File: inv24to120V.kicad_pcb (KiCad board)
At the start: 2 copper layers, 105 x 155 mm, 133 parts, among them IC1 FSAM50SM60A, J1 Conn_02x13_Odd_Even_MountingP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, J10 Screw_Terminal_01x01, J11 Screw_Terminal_01x01, J12 Screw_Terminal_01x01, J2 Conn_02x13_Odd_Even_MountingP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, J3 Screw_Terminal_01x01, J4 Conn_02x05_Odd_Even_MountingP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, J5 Screw_Terminal_01x02, J6 Screw_Terminal_01x03, J7 Screw_Terminal_01x03, J8 Screw_Terminal_01x03, J9 Screw_Terminal_01x02, K1 J0971CS5VDC.45, Q1 IRFZ44NPBF, Q2 IRFZ44NPBF, Q3 2SC1815, Q4 2SC1815, Q5 2SA1015, Q6 2SA1015, Q7 2SC1815, U1 ESP32-DEVKITC-32D, U10 PC817, U2 LM2576HVT-5, U3 ACS712ELCTR30AT, U4 ACS712ELCTR30AT, U5 LM2576HVT-5, U6 ISO7340CDW, U7 ISO7340CDW, U8 AMC1300BDWVR, U9 PC817

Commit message: start rout
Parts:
- removed J1, J2: Conn_02x13_Odd_Even_MountingPin, Connector_IDC:IDC-Header_2x13_P2.54mm_Vertical
- removed J10, J11, J12, J3: Screw_Terminal_01x01, TerminalBlock_Wuerth:Wuerth_REDCUBE-THR_WP-THRBU_74650073_THR
- C10, C11, C12, C24, C25, C26, C27, C28, C29, C30, C31, C33, C34, C5, C6, C7, C8, C9: footprint Capacitor_SMD:C_0805_2012Metric -> Capacitor_SMD:C_0805_2012Metric_Pad1.18x1.45mm_HandSolder
- C13, C14, C15: footprint Capacitor_SMD:C_0805_2012Metric -> Capacitor_SMD:C_1206_3216Metric_Pad1.33x1.80mm_HandSolder
- R10, R22, R23, R24, R25, R26, R27, R28, R29, R30, R31, R32, R33, R34, R35, R36, R37, R7, R8, R9: footprint Resistor_SMD:R_0805_2012Metric -> Resistor_SMD:R_0805_2012Metric_Pad1.20x1.40mm_HandSolder
- R40, R44: footprint Resistor_THT:R_Axial_DIN0207_L6.3mm_D2.5mm_P10.16mm_Horizontal -> Resistor_SMD:R_0805_2012Metric_Pad1.20x1.40mm_HandSolder
- U1: footprint inv24VLib:MODULE_ESP32-DEVKITC-32D -> Connector_PinSocket_2.54mm:PinSocket_2x20_P2.54mm_Vertical
- moved J6 208.6 mm to (149.0, 160.0)
- moved Q7 204.7 mm to (127.5, 166.0)
- moved BX1 204.1 mm to (140.8, 175.0)
- moved D7 195.0 mm to (112.9, 176.0)
- moved BX2 190.3 mm to (126.9, 175.0)
- moved R42 181.8 mm to (135.0, 160.8), turned to -90 degrees
- moved R48 180.6 mm to (139.0, 161.0), turned to -90 degrees
- moved U9 162.5 mm to (114.2, 168.7)
- moved R46 162.0 mm to (109.8, 164.0)
- moved R45 158.4 mm to (95.8, 164.0)
- moved J9 158.1 mm to (102.0, 175.1), turned to 90 degrees
- moved K1 151.1 mm to (80.7, 143.7)
- moved R47 146.3 mm to (93.0, 177.0), turned to 90 degrees
- moved U10 139.7 mm to (116.3, 85.2), turned to -90 degrees
- moved C13 127.8 mm to (84.0, 71.5), turned to 180 degrees
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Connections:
- BX4 pad 2: VTH_IPM1 -> VTH_IPM
- BX6 pad 1: TEMPERATURE_IPM2 -> TEMPERATURE_IPM
- C33 pad 2: VTH_IPM1 -> VTH_IPM
- C34 pad 2: TEMPERATURE_IPM2 -> TEMPERATURE_IPM
- C35 pad 1: VTH_IPM1 -> VTH_IPM
- D8 pad 2: 150V_OUT1 -> 150V_OUT
- IC1 pad 16: unconnected-(IC1-COM(H)-Pad16) -> GNDPWR
- IC1 pad 24: VTH_IPM2 -> VTH_IPM
- IC1 pad 32: 150V_OUT -> VBUS
- L4 pad 1: Net-(J12-Pin_1) -> VBUS
- R10 pad 2: I_Vphase2 -> I_Vphase
- R17 pad 2: Net-(J12-Pin_1) -> VBUS
- R19 pad 1: GNDPWR1 -> GNDPWR
- R29 pad 1: UH2 -> Net-(U6-OUTA)
- R30 pad 1: VH2 -> Net-(U6-OUTB)
- R31 pad 1: WH2 -> Net-(U6-OUTC)
- R32 pad 1: UL2 -> Net-(U7-OUTA)
- R33 pad 1: VL2 -> Net-(U7-OUTB)
- R34 pad 1: WL2 -> Net-(U7-OUTC)
- R40 pad 2: TEMPERATURE_IPM2 -> TEMPERATURE_IPM
- R44 pad 2: FAULT_IPM2 -> FAULT_IPM
- R7 pad 1: I_Uphase2 -> I_Uphase
- R8 pad 1: I_Vphase2 -> I_Vphase
- R9 pad 2: I_Uphase2 -> I_Uphase
- U10 pad 4: FAULT_IPM2 -> FAULT_IPM
- U6 pad 12: WH1 -> Net-(U6-OUTC)
- U6 pad 13: VH1 -> Net-(U6-OUTB)
- U6 pad 14: UH1 -> Net-(U6-OUTA)
- U7 pad 12: WL1 -> Net-(U7-OUTC)
- U7 pad 13: VL1 -> Net-(U7-OUTB)
- U7 pad 14: UL1 -> Net-(U7-OUTA)
- U8 pad 3: GNDPWR1 -> GNDPWR
- X1 pad 12: GNDPWR1 -> GNDPWR
- X1 pad 13: GNDPWR1 -> GNDPWR
- X1 pad 15: 150V_OUT1 -> 150V_OUT
- X1 pad 16: 150V_OUT1 -> 150V_OUT

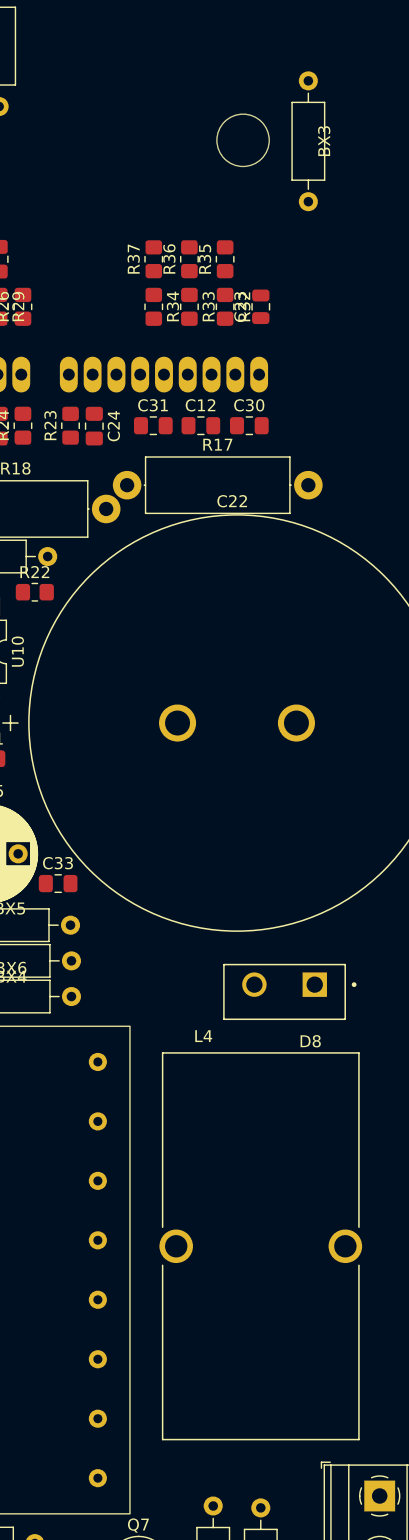
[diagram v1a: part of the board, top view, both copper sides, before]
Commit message: add class name
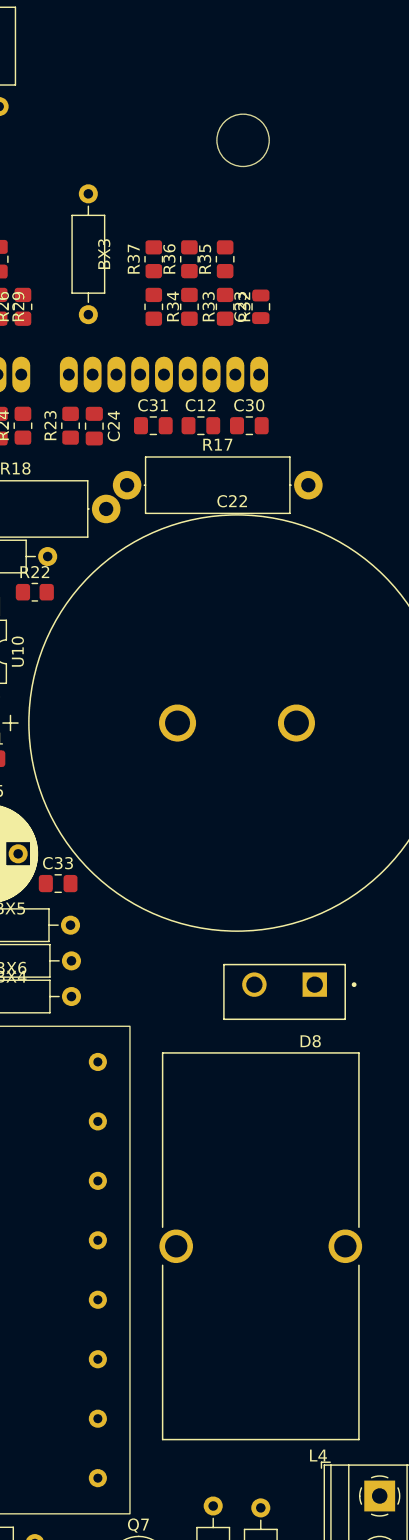
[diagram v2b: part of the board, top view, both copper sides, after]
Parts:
- moved BX3 20.8 mm to (124.5, 60.7)
- turned L4 to 180 degrees
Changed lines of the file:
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@@
   )
   (footprint "inv24VLib:IND_HCTI-10-20.0" (layer "F.Cu")
-    (at 139 139)
+    (at 139 139 180)
     (property "Sheetfile" "inv24to120V.kicad_sch")
     (property "Sheetname" "")
@@
     (fp_line (start 8.255 16.256) (end -8.255 16.256)
       (stroke (width 0.127) (type solid)) (layer "F.Fab"))
-    (pad "1" thru_hole circle (at -7.112 0) (size 2.82 2.82) (drill 1.88) (layers "*.Cu" "*.Mask")
+    (pad "1" thru_hole circle (at -7.112 0 180) (size 2.82 2.82) (drill 1.88) (layers "*.Cu" "*.Mask")
       (net 80 "VBUS") (pinfunction "1") (pintype "passive") (solder_mask_margin 0.102))
-    (pad "2" thru_hole circle (at 7.112 0) (size 2.82 2.82) (drill 1.88) (layers "*.Cu" "*.Mask")
+    (pad "2" thru_hole circle (at 7.112 0 180) (size 2.82 2.82) (drill 1.88) (layers "*.Cu" "*.Mask")
       (net 87 "Net-(D8-K)") (pinfunction "2") (pintype "passive") (solder_mask_margin 0.102))
     (model "${KIPRJMOD}/inv24VLib/ATCA-08-471M-V.STEP"
@@
   )
   (footprint "Resistor_THT:R_Axial_DIN0207_L6.3mm_D2.5mm_P10.16mm_Horizontal" (layer "F.Cu")
-    (at 143 51.16 90)
+    (at 124.5 60.66 90)
     (descr "Resistor, Axial_DIN0207 series, Axial, Horizontal, pin pitch=10.16mm, 0.25W = 1/4W, length*diameter=6.3*2.5mm^2, http://cdn-reichelt.de/documents/datenblatt/B400/1_4W%23YAG.pdf")
     (tags "Resistor Axial_DIN0207 series Axial Horizontal pin pitch 10.16mm 0.25W = 1/4W length 6.3mm diameter 2.5mm")

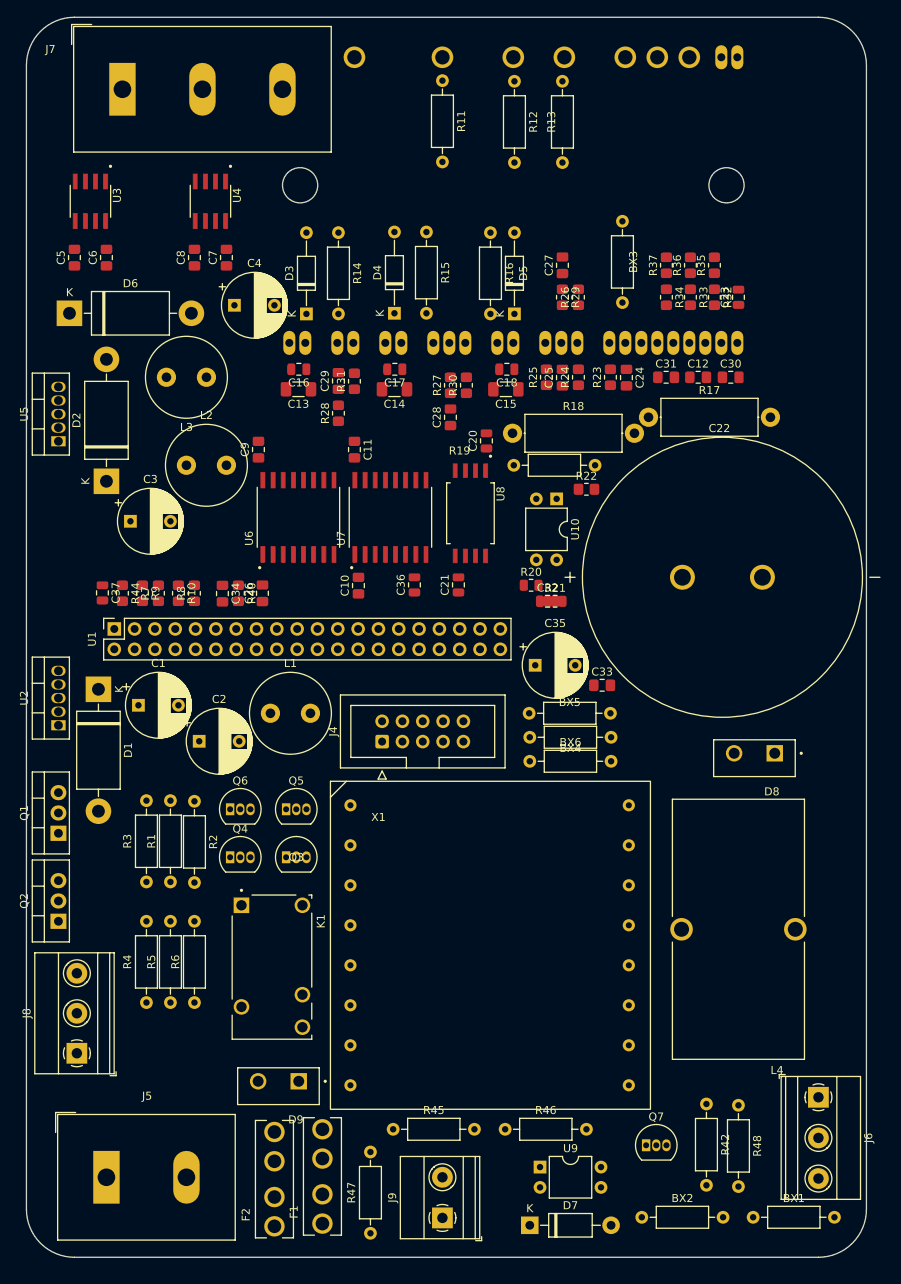
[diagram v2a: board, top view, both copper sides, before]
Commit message: remove aux addon connect
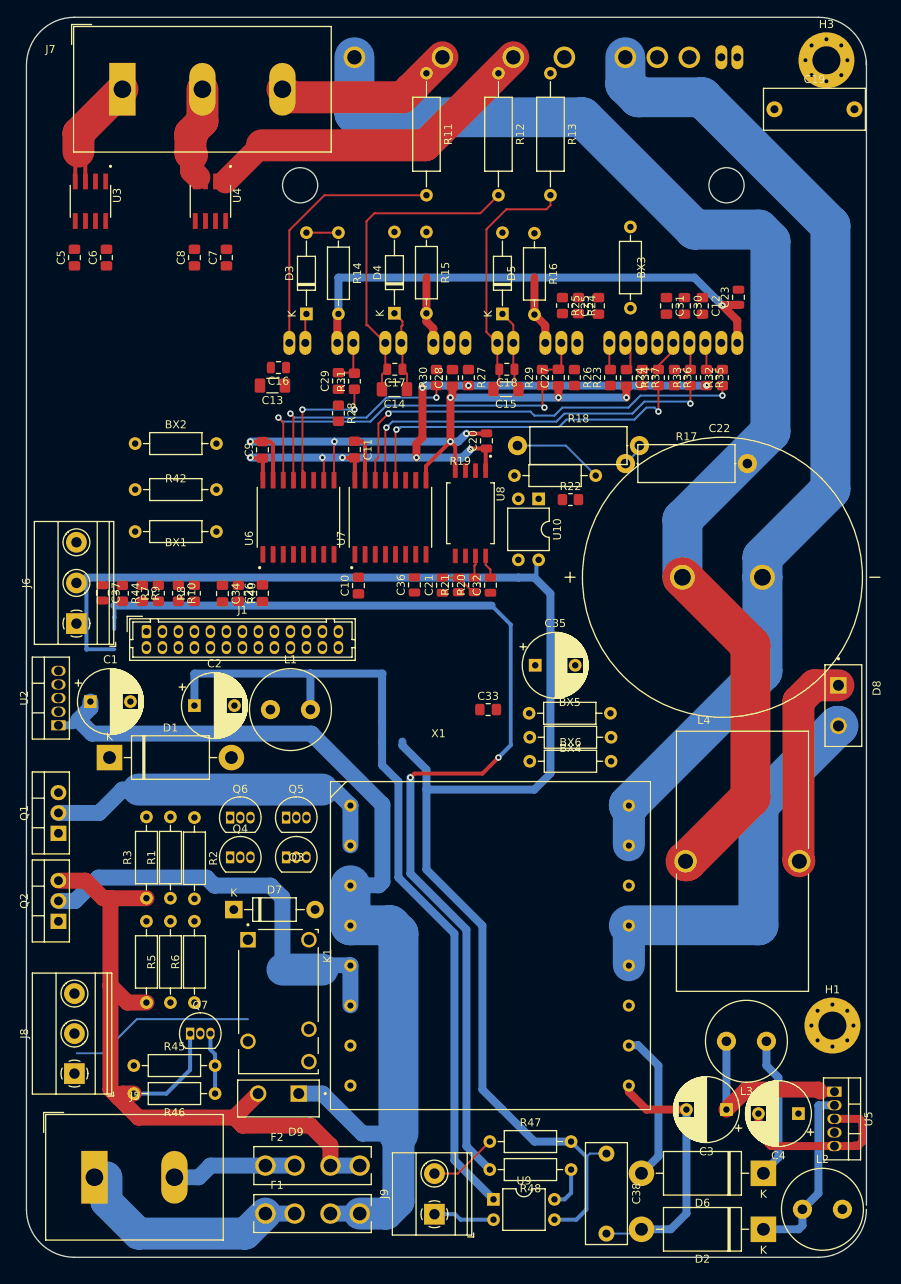
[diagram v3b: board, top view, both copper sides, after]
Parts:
- removed J4: Conn_02x05_Odd_Even_MountingPin, Connector_IDC:IDC-Header_2x05_P2.54mm_Vertical
- removed U1: ESP32-DEVKITC-32D, Connector_PinSocket_2.54mm:PinSocket_2x20_P2.54mm_Vertical
- added C19: 102, Capacitor_THT:C_Disc_D12.5mm_W5.0mm_P10.00mm, F.Cu at (143.5, 36.5)
- added C38: 102, Capacitor_THT:C_Disc_D12.5mm_W5.0mm_P10.00mm, F.Cu at (122.5, 167.0)
- added H1: MountingHole_Pad, MountingHole:MountingHole_3.5mm_Pad_Via, F.Cu at (150.8, 151.0)
- added H3: MountingHole_Pad, MountingHole:MountingHole_3.5mm_Pad_Via, F.Cu at (150.0, 30.4)
- added J1: Conn_02x13_Odd_Even, Connector_Hirose:Hirose_DF11-26DP-2DSA_2x13_P2.00mm_Vertical, F.Cu at (65.0, 101.8)
- R11, R12, R13: footprint Resistor_THT:R_Axial_DIN0207_L6.3mm_D2.5mm_P10.16mm_Horizontal -> Resistor_THT:R_Axial_DIN0309_L9.0mm_D3.2mm_P15.24mm_Horizontal
- moved D6 138.1 mm to (142.1, 169.5), turned to 180 degrees
- moved U5 126.6 mm to (151.0, 159.3), turned to -90 degrees
- moved D2 124.4 mm to (142.1, 176.5), turned to 180 degrees
- moved C4 123.2 mm to (146.5, 162.0), turned to 180 degrees
- moved L2 120.7 mm to (147.0, 174.0)
- moved BX2 115.6 mm to (63.6, 78.3)
- moved BX1 115.4 mm to (63.6, 89.3)
- moved J6 110.0 mm to (56.2, 100.8), turned to 90 degrees
- moved L3 108.6 mm to (142.5, 153.0)
- moved C3 104.7 mm to (137.5, 161.5), turned to 180 degrees
- moved R42 98.2 mm to (73.8, 84.0), turned to 180 degrees
- moved Q7 58.7 mm to (70.5, 152.0)
- moved D7 54.1 mm to (75.9, 136.5)
- moved R46 36.5 mm to (73.6, 159.5), turned to 180 degrees
- moved R45 33.4 mm to (63.4, 156.0)
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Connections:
- net Net-(Q1-D) renamed /pri1
- net Net-(Q2-D) renamed /pri2
- X1 pad 12: GNDPWR -> 150V_OUT
- X1 pad 13: GNDPWR -> 150V_OUT
- X1 pad 15: 150V_OUT -> GNDPWR
- X1 pad 16: 150V_OUT -> GNDPWR
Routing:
- net GND: track 0.00 -> 288.0 mm
- net VBUS: track 0.00 -> 154.6 mm
- net GND2: track 0.00 -> 145.6 mm, vias 0 -> 7
- net +3.3V: track 0.00 -> 135.9 mm, vias 0 -> 2
- net +24V: track 0.00 -> 130.5 mm
- net GNDPWR: track 0.00 -> 124.2 mm
- net +5V: track 0.00 -> 106.5 mm
- net +15V: track 0.00 -> 105.6 mm, vias 0 -> 1
- net +5VP: track 0.00 -> 89.6 mm, vias 0 -> 8
- net Net-(U7-OUTA): track 0.00 -> 53.7 mm, vias 0 -> 2
- net /pri2: track 0.00 -> 53.0 mm
- net 150V_OUT: track 0.00 -> 50.3 mm
- net Net-(U7-OUTB): track 0.00 -> 48.3 mm, vias 0 -> 2
- net Net-(U6-OUTA): track 0.00 -> 45.3 mm, vias 0 -> 2
- net Net-(U7-OUTC): track 0.00 -> 43.7 mm, vias 0 -> 2
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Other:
- outline, holes or cut-outs redrawn

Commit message: place parts
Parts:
- moved Q7 89.3 mm to (75.5, 62.9)
- moved K1 86.6 mm to (60.5, 64.0), turned to 180 degrees
- moved R46 84.5 mm to (73.1, 75.0)
- moved R45 84.0 mm to (63.2, 72.0)
- moved D7 76.6 mm to (73.0, 60.0), turned to -90 degrees
- moved J8 73.5 mm to (56.1, 83.5)
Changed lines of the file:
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@@
   (net 104 "Earth_Protective")
   (footprint "TerminalBlock_Phoenix:TerminalBlock_Phoenix_MKDS-1,5-3_1x03_P5.00mm_Horizontal" (layer "F.Cu")
-    (at 56 157.0375 90)
+    (at 56.055 83.5375 90)
     (descr "Terminal Block Phoenix MKDS-1,5-3, 3 pins, pitch 5mm, size 15x9.8mm^2, drill diamater 1.3mm, pad diameter 2.6mm, see http://www.farnell.com/datasheets/100425.pdf, script-generated using https://github.com/pointhi/kicad-footprint-generator/scripts/TerminalBlock_Phoenix")
     (tags "THT Terminal Block Phoenix MKDS-1,5-3 pitch 5mm size 15x9.8mm^2 drill 1.3mm pad 2.6mm")
@@
   )
   (footprint "Diode_THT:D_DO-41_SOD81_P10.16mm_Horizontal" (layer "F.Cu")
-    (at 75.92 136.5375)
+    (at 73 60.0375 -90)
     (descr "Diode, DO-41_SOD81 series, Axial, Horizontal, pin pitch=10.16mm, , length*diameter=5.2*2.7mm^2, , http://www.diodes.com/_files/packages/DO-41%20(Plastic).pdf")
     (tags "Diode DO-41_SOD81 series Axial Horizontal pin pitch 10.16mm  length 5.2mm diameter 2.7mm")
@@
     (property "ki_keywords" "diode")
     (attr through_hole)
-    (fp_text reference "D7" (at 5.08 -2.47) (layer "F.SilkS")
+    (fp_text reference "D7" (at 5.08 -2.47 90) (layer "F.SilkS")
         (effects (font (size 1 1) (thickness 0.15)))
     )
-    (fp_text value "1N4002" (at 5.08 2.47) (layer "F.Fab")
+    (fp_text value "1N4002" (at 5.08 2.47 90) (layer "F.Fab")
         (effects (font (size 1 1) (thickness 0.15)))
     )
-    (fp_text user "K" (at 0 -2.1) (layer "F.SilkS")
+    (fp_text user "K" (at 0 -2.1 90) (layer "F.SilkS")
         (effects (font (size 1 1) (thickness 0.15)))
     )
-    (fp_text user "${REFERENCE}" (at 5.47 0) (layer "F.Fab")
+    (fp_text user "${REFERENCE}" (at 5.47 0 90) (layer "F.Fab")
         (effects (font (size 1 1) (thickness 0.15)))
     )
-    (fp_text user "K" (at 0 -2.1) (layer "F.Fab")
+    (fp_text user "K" (at 0 -2.1 90) (layer "F.Fab")
         (effects (font (size 1 1) (thickness 0.15)))
     )
@@
     (fp_line (start 10.16 0) (end 7.68 0)
       (stroke (width 0.1) (type solid)) (layer "F.Fab"))
-    (pad "1" thru_hole rect (at 0 0) (size 2.2 2.2) (drill 1.1) (layers "*.Cu" "*.Mask")
+    (pad "1" thru_hole rect (at 0 0 270) (size 2.2 2.2) (drill 1.1) (layers "*.Cu" "*.Mask")
       (net 17 "+5V") (pinfunction "K") (pintype "passive"))
-    (pad "2" thru_hole oval (at 10.16 0) (size 2.2 2.2) (drill 1.1) (layers "*.Cu" "*.Mask")
+    (pad "2" thru_hole oval (at 10.16 0 270) (size 2.2 2.2) (drill 1.1) (layers "*.Cu" "*.Mask")
       (net 41 "Net-(D7-A)") (pinfunction "A") (pintype "passive"))
     (model "${KICAD6_3DMODEL_DIR}/Diode_THT.3dshapes/D_DO-41_SOD81_P10.16mm_Horizontal.wrl"
@@
   )
   (footprint "Resistor_THT:R_Axial_DIN0207_L6.3mm_D2.5mm_P10.16mm_Horizontal" (layer "F.Cu")
-    (at 73.58 159.5375 180)
+    (at 73.08 75.0375 180)
     (descr "Resistor, Axial_DIN0207 series, Axial, Horizontal, pin pitch=10.16mm, 0.25W = 1/4W, length*diameter=6.3*2.5mm^2, http://cdn-reichelt.de/documents/datenblatt/B400/1_4W%23YAG.pdf")
     (tags "Resistor Axial_DIN0207 series Axial Horizontal pin pitch 10.16mm 0.25W = 1/4W length 6.3mm diameter 2.5mm")
@@
   )
   (footprint "Resistor_THT:R_Axial_DIN0207_L6.3mm_D2.5mm_P10.16mm_Horizontal" (layer "F.Cu")
-    (at 63.42 156.0375)
+    (at 63.17 72.0375)
     (descr "Resistor, Axial_DIN0207 series, Axial, Horizontal, pin pitch=10.16mm, 0.25W = 1/4W, length*diameter=6.3*2.5mm^2, http://cdn-reichelt.de/documents/datenblatt/B400/1_4W%23YAG.pdf")
     (tags "Resistor Axial_DIN0207 series Axial Horizontal pin pitch 10.16mm 0.25W = 1/4W length 6.3mm diameter 2.5mm")
@@
   )
   (footprint "Package_TO_SOT_THT:TO-92_Inline" (layer "F.Cu")
-    (at 70.46 152.0375)
+    (at 75.48 62.8975)
     (descr "TO-92 leads in-line, narrow, oval pads, drill 0.75mm (see NXP sot054_po.pdf)")
     (tags "to-92 sc-43 sc-43a sot54 PA33 transistor")
@@
   )
   (footprint "inv24VLib:RELAY_J0971CS5VDC.45" (layer "F.Cu")
-    (at 81.5 148.0375 -90)
+    (at 60.5 64.0375 180)
     (property "Availability" "In Stock")
     (property "Check_prices" "https://www.snapeda.com/parts/J0971CS5VDC.45/CIT+Relay+%2526+Switch/view-part/?ref=eda")
@@
     (property "SnapEDA_Link" "https://www.snapeda.com/parts/J0971CS5VDC.45/CIT+Relay+%2526+Switch/view-part/?ref=snap")
     (attr through_hole)
-    (fp_text reference "K1" (at -5.725 -6.135 90) (layer "F.SilkS")
+    (fp_text reference "K1" (at -5.725 -6.135) (layer "F.SilkS")
         (effects (font (size 1 1) (thickness 0.15)))
     )
-    (fp_text value "J0971CS5VDC.45" (at 3.8 6.13 90) (layer "F.Fab")
+    (fp_text value "J0971CS5VDC.45" (at 3.8 6.13) (layer "F.Fab")
         (effects (font (size 1 1) (thickness 0.15)))
     )
@@
     (fp_circle (center -9.6 3.81) (end -9.5 3.81)
       (stroke (width 0.2) (type solid)) (fill none) (layer "F.Fab"))
-    (pad "11" thru_hole circle (at 4.97 3.81 270) (size 1.95 1.95) (drill 1.3) (layers "*.Cu" "*.Mask")
+    (pad "11" thru_hole circle (at 4.97 3.81 180) (size 1.95 1.95) (drill 1.3) (layers "*.Cu" "*.Mask")
       (net 52 "Net-(J8-Pin_1)") (pintype "passive") (solder_mask_margin 0.102))
-    (pad "12" thru_hole circle (at 3.446 -3.81 270) (size 1.95 1.95) (drill 1.3) (layers "*.Cu" "*.Mask")
+    (pad "12" thru_hole circle (at 3.446 -3.81 180) (size 1.95 1.95) (drill 1.3) (layers "*.Cu" "*.Mask")
       (net 57 "Net-(J8-Pin_3)") (pintype "passive") (solder_mask_margin 0.102))
-    (pad "14" thru_hole circle (at 7.51 -3.81 270) (size 1.95 1.95) (drill 1.3) (layers "*.Cu" "*.Mask")
+    (pad "14" thru_hole circle (at 7.51 -3.81 180) (size 1.95 1.95) (drill 1.3) (layers "*.Cu" "*.Mask")
       (net 53 "Net-(J8-Pin_2)") (pintype "passive") (solder_mask_margin 0.102))
-    (pad "A1" thru_hole rect (at -7.73 3.81 270) (size 1.95 1.95) (drill 1.3) (layers "*.Cu" "*.Mask")
+    (pad "A1" thru_hole rect (at -7.73 3.81 180) (size 1.95 1.95) (drill 1.3) (layers "*.Cu" "*.Mask")
       (net 17 "+5V") (pintype "passive") (solder_mask_margin 0.102))
-    (pad "A2" thru_hole circle (at -7.73 -3.81 270) (size 1.95 1.95) (drill 1.3) (layers "*.Cu" "*.Mask")
+    (pad "A2" thru_hole circle (at -7.73 -3.81 180) (size 1.95 1.95) (drill 1.3) (layers "*.Cu" "*.Mask")
       (net 41 "Net-(D7-A)") (pintype "passive") (solder_mask_margin 0.102))
     (model "${KIPRJMOD}/inv24VLib/J0971CS5VDC.45--3DModel-STEP-56544.STEP"
